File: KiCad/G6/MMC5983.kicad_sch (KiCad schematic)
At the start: 3 parts, among them U4 MMC5983MA-Magnetomer

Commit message: i finally finished routing everything to spi
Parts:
- C4: footprint CC0805KK7R7BB225:CAP_CC0805_YAG -> CC0603KRXQRQBB104:10CAPC370195_195N_KEM-L
- C5: footprint CC0603KRX7R7BB105:YAG_CC0603_YAG -> CC0603KRXQRQBB104:1CAP_CS1206_YAG
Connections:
- net 3.3v: no longer U4.4 (~{SPI_CS})
- net SPI-SDO-MAIN: now reaches U4.5 (SPI_SDO)
- net I2C-SCL-MAIN renamed SPI-SCK-MAIN
- net I2C-SDA-MAIN renamed SPI-SDI-MAIN
- new net CS-MMC: U4.4 (~{SPI_CS})
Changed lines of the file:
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@@
 	(paper "A4")
-	(junction
-		(at 171.45 83.82)
-		(diameter 0)
-		(color 0 0 0 0)
-	)
 	(junction
 		(at 158.75 81.28)
@@
 	(wire
 		(pts
-			(xy 154.94 83.82) (xy 171.45 83.82)
+			(xy 154.94 83.82) (xy 181.61 83.82)
 		)
 		(stroke
@@
 	(wire
 		(pts
-			(xy 105.41 59.69) (xy 105.41 86.36)
+			(xy 106.68 99.06) (xy 114.3 99.06)
 		)
 		(stroke
@@
 	(wire
 		(pts
-			(xy 106.68 99.06) (xy 114.3 99.06)
+			(xy 154.94 81.28) (xy 158.75 81.28)
 		)
 		(stroke
@@
 	(wire
 		(pts
-			(xy 154.94 81.28) (xy 158.75 81.28)
+			(xy 158.75 76.2) (xy 158.75 81.28)
 		)
 		(stroke
@@
 	(wire
 		(pts
-			(xy 171.45 59.69) (xy 171.45 83.82)
+			(xy 90.17 88.9) (xy 114.3 88.9)
 		)
 		(stroke
@@
 	(wire
 		(pts
-			(xy 171.45 83.82) (xy 181.61 83.82)
+			(xy 158.75 81.28) (xy 163.83 81.28)
 		)
 		(stroke
@@
 		)
 	)
-	(wire
-		(pts
-			(xy 158.75 76.2) (xy 158.75 81.28)
-		)
-		(stroke
-			(width 0)
-			(type default)
-		)
-	)
-	(wire
-		(pts
-			(xy 90.17 88.9) (xy 114.3 88.9)
-		)
-		(stroke
-			(width 0)
-			(type default)
-		)
-	)
-	(wire
-		(pts
-			(xy 105.41 86.36) (xy 114.3 86.36)
-		)
-		(stroke
-			(width 0)
-			(type default)
-		)
-	)
-	(wire
-		(pts
-			(xy 158.75 81.28) (xy 163.83 81.28)
-		)
-		(stroke
-			(width 0)
-			(type default)
-		)
-	)
-	(wire
-		(pts
-			(xy 105.41 59.69) (xy 171.45 59.69)
-		)
-		(stroke
-			(width 0)
-			(type default)
-		)
-	)
-	(global_label "I2C-SDA-MAIN"
+	(global_label "SPI-SDI-MAIN"
 		(shape input)
 		(at 88.9 91.44 180)
@@
 		)
 		(property "Intersheetrefs" "${INTERSHEET_REFS}"
-			(at 71.6423 91.44 0)
+			(at 72.1261 91.44 0)
 			(effects
 				(font
@@
 		)
 	)
-	(global_label "I2C-SCL-MAIN"
+	(global_label "SPI-SCK-MAIN"
 		(shape input)
 		(at 90.17 88.9 180)
@@
 		)
 		(property "Intersheetrefs" "${INTERSHEET_REFS}"
-			(at 72.9728 88.9 0)
+			(at 72.7309 88.9 0)
+			(effects
+				(font
+					(size 1.27 1.27)
+				)
+				(justify right)
+				(hide yes)
+			)
+		)
+	)
+	(global_label "SPI-SDO-MAIN"
+		(shape input)
+		(at 114.3 93.98 180)
+		(fields_autoplaced yes)
+		(effects
+			(font
+				(size 1.27 1.27)
+			)
+			(justify right)
+		)
+		(property "Intersheetrefs" "${INTERSHEET_REFS}"
+			(at 96.8004 93.98 0)
 			(effects
 				(font
@@
 				)
 				(justify left)
+				(hide yes)
+			)
+		)
+	)
+	(global_label "CS-MMC"
+		(shape input)
+		(at 114.3 86.36 180)
+		(fields_autoplaced yes)
+		(effects
+			(font
+				(size 1.27 1.27)
+			)
+			(justify right)
+		)
+		(property "Intersheetrefs" "${INTERSHEET_REFS}"
+			(at 103.0901 86.36 0)
+			(effects
+				(font
+					(size 1.27 1.27)
+				)
+				(justify right)
 				(hide yes)
 			)
@@
 			)
 		)
-		(property "Footprint" "CC0805KK7R7BB225:CAP_CC0805_YAG"
+		(property "Footprint" "CC0603KRXQRQBB104:10CAPC370195_195N_KEM-L"
 			(at 106.68 99.06 0)
 			(effects
@@
 			)
 		)
-		(property "Footprint" "CC0603KRX7R7BB105:YAG_CC0603_YAG"
+		(property "Footprint" "CC0603KRXQRQBB104:1CAP_CS1206_YAG"
 			(at 158.75 76.2 0)
 			(effects

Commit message: uhhhh im confused gang
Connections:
- net SPI-SDI-MAIN renamed SPI-SDI-MMC
- net SPI-SDO-MAIN renamed SPI-SDO-MMC
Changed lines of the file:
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@@
 		)
 	)
-	(global_label "SPI-SDI-MAIN"
+	(global_label "SPI-SDI-MMC"
 		(shape input)
 		(at 88.9 91.44 180)
@@
 		)
 		(property "Intersheetrefs" "${INTERSHEET_REFS}"
-			(at 72.1261 91.44 0)
+			(at 72.4286 91.44 0)
 			(effects
 				(font
@@
 		)
 	)
-	(global_label "SPI-SDO-MAIN"
+	(global_label "SPI-SDO-MMC"
 		(shape input)
 		(at 114.3 93.98 180)
@@
 		)
 		(property "Intersheetrefs" "${INTERSHEET_REFS}"
-			(at 96.8004 93.98 0)
+			(at 97.1029 93.98 0)
 			(effects
 				(font

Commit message: I think the schematics done uhhh idrk
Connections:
- net SPI-SCK-MAIN renamed SCK-MAIN
- net SPI-SDI-MMC renamed MOSI-MMC
- net SPI-SDO-MMC renamed MISO-MMC
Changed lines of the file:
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@@
-		)
-	)
-	(global_label "SPI-SDI-MMC"
-		(shape input)
-		(at 88.9 91.44 180)
-		(fields_autoplaced yes)
-		(effects
-			(font
-				(size 1.27 1.27)
-			)
-			(justify right)
-		)
-		(property "Intersheetrefs" "${INTERSHEET_REFS}"
-			(at 72.4286 91.44 0)
-			(effects
-				(font
-					(size 1.27 1.27)
-				)
-				(justify right)
-				(hide yes)
-			)
 		)
 	)
@@
 				)
 				(justify left)
-				(hide yes)
-			)
-		)
-	)
-	(global_label "SPI-SCK-MAIN"
-		(shape input)
-		(at 90.17 88.9 180)
-		(fields_autoplaced yes)
-		(effects
-			(font
-				(size 1.27 1.27)
-			)
-			(justify right)
-		)
-		(property "Intersheetrefs" "${INTERSHEET_REFS}"
-			(at 72.7309 88.9 0)
-			(effects
-				(font
-					(size 1.27 1.27)
-				)
-				(justify right)
-				(hide yes)
-			)
-		)
-	)
-	(global_label "SPI-SDO-MMC"
-		(shape input)
-		(at 114.3 93.98 180)
-		(fields_autoplaced yes)
-		(effects
-			(font
-				(size 1.27 1.27)
-			)
-			(justify right)
-		)
-		(property "Intersheetrefs" "${INTERSHEET_REFS}"
-			(at 97.1029 93.98 0)
-			(effects
-				(font
-					(size 1.27 1.27)
-				)
-				(justify right)
 				(hide yes)
 			)
@@
 		)
 	)
-	(global_label "CS-MMC"
+	(hierarchical_label "SCK-MAIN"
 		(shape input)
-		(at 114.3 86.36 180)
-		(fields_autoplaced yes)
+		(at 90.17 88.9 180)
 		(effects
 			(font
@@
 			(justify right)
 		)
-		(property "Intersheetrefs" "${INTERSHEET_REFS}"
-			(at 103.0901 86.36 0)
-			(effects
-				(font
-					(size 1.27 1.27)
-				)
-				(justify right)
-				(hide yes)
+	)
+	(hierarchical_label "MOSI-MMC"
+		(shape input)
+		(at 88.9 91.44 180)
+		(effects
+			(font
+				(size 1.27 1.27)
 			)
+			(justify right)
 		)
 	)
+	(hierarchical_label "MISO-MMC"
+		(shape input)
+		(at 114.3 93.98 180)
+		(effects
+			(font
+				(size 1.27 1.27)
+			)
+			(justify right)
+		)
+	)
+	(hierarchical_label "CS-MMC"
+		(shape input)
+		(at 114.3 86.36 180)
+		(effects
+			(font
+				(size 1.27 1.27)
+			)
+			(justify right)
+		)
+	)

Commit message: im sorry parsa :/
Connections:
- net INT-MMC: no longer names the net of U4.15 (INT)
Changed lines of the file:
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@@
-		)
-	)
-	(global_label "INT-MMC"
-		(shape input)
-		(at 154.94 91.44 0)
-		(fields_autoplaced yes)
-		(effects
-			(font
-				(size 1.27 1.27)
-			)
-			(justify left)
-		)
-		(property "Intersheetrefs" "${INTERSHEET_REFS}"
-			(at 166.5733 91.44 0)
-			(effects
-				(font
-					(size 1.27 1.27)
-				)
-				(justify left)
-				(hide yes)
-			)
 		)
 	)

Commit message: sasha sneaky academic
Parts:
- renumbered U4 to U6
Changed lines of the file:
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@@
 		(dnp no)
 		(fields_autoplaced yes)
-		(property "Reference" "#PWR013"
+		(property "Reference" "#PWR030"
 			(at 106.68 113.03 0)
 			(effects
@@
 			(project "G6"
 				(path "/99017594-210d-4d15-87a7-3152ef0d7b7c/f6567545-cc19-4658-bc7a-b618e0397156"
-					(reference "#PWR013")
+					(reference "#PWR030")
 					(unit 1)
 				)
@@
 		(dnp no)
 		(fields_autoplaced yes)
-		(property "Reference" "#PWR016"
+		(property "Reference" "#PWR033"
 			(at 158.75 62.23 0)
 			(effects
@@
 			(project "G6"
 				(path "/99017594-210d-4d15-87a7-3152ef0d7b7c/f6567545-cc19-4658-bc7a-b618e0397156"
-					(reference "#PWR016")
+					(reference "#PWR033")
 					(unit 1)
 				)
@@
 		(on_board yes)
 		(dnp no)
-		(property "Reference" "U4"
+		(property "Reference" "U6"
 			(at 134.62 73.66 0)
 			(effects
@@
 			(project "G6"
 				(path "/99017594-210d-4d15-87a7-3152ef0d7b7c/f6567545-cc19-4658-bc7a-b618e0397156"
-					(reference "U4")
+					(reference "U6")
 					(unit 1)
 				)
@@
 		(dnp no)
 		(fields_autoplaced yes)
-		(property "Reference" "#PWR015"
+		(property "Reference" "#PWR032"
 			(at 161.29 121.92 0)
 			(effects
@@
 			(project "G6"
 				(path "/99017594-210d-4d15-87a7-3152ef0d7b7c/f6567545-cc19-4658-bc7a-b618e0397156"
-					(reference "#PWR015")
+					(reference "#PWR032")
 					(unit 1)
 				)
@@
 		(dnp no)
 		(fields_autoplaced yes)
-		(property "Reference" "#PWR014"
+		(property "Reference" "#PWR031"
 			(at 161.29 119.38 0)
 			(effects
@@
 			(project "G6"
 				(path "/99017594-210d-4d15-87a7-3152ef0d7b7c/f6567545-cc19-4658-bc7a-b618e0397156"
-					(reference "#PWR014")
-					(unit 1)
-				)
+					(reference "#PWR031")
+					(unit 1)
+				)

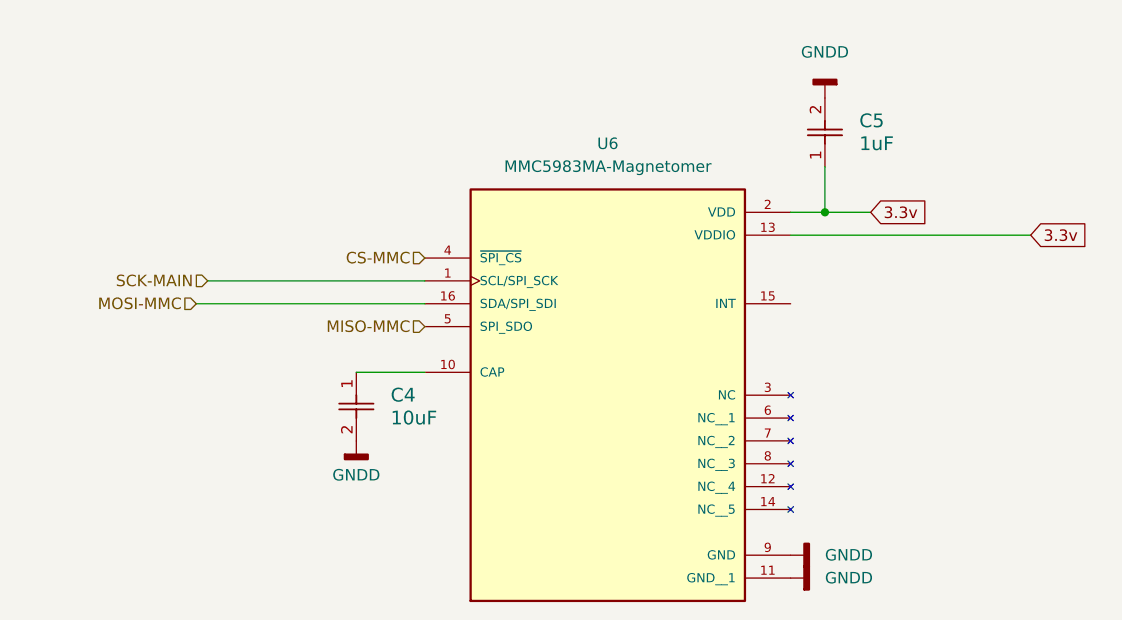
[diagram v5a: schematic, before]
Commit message: errrrrr i cant find a umcx connector they all say there like $50??
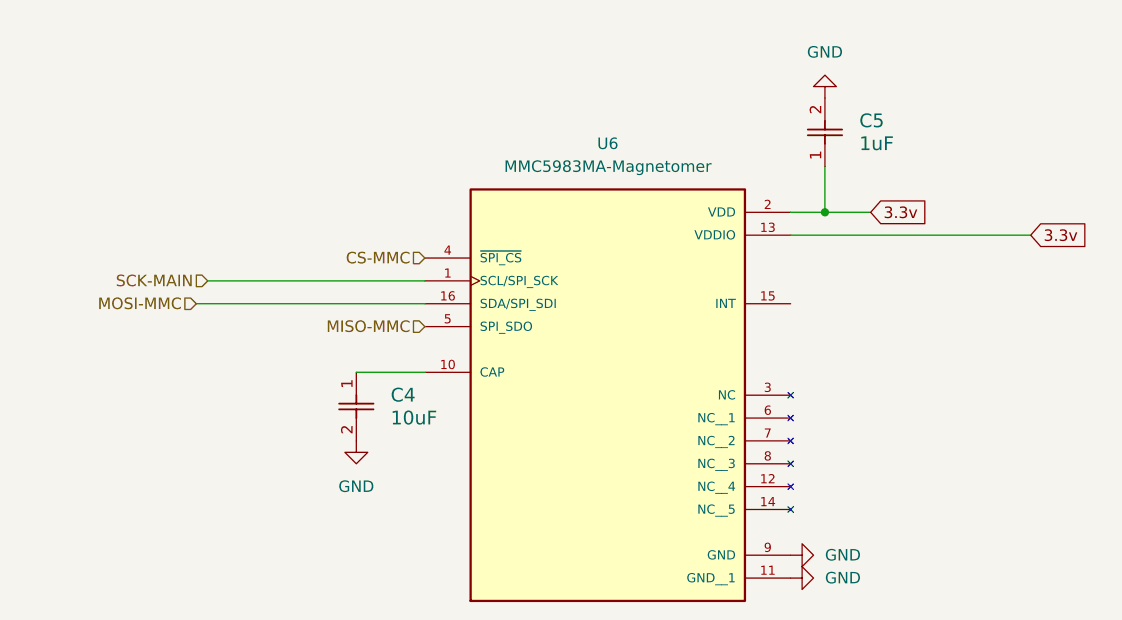
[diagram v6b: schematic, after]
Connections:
- net GNDD renamed GND
